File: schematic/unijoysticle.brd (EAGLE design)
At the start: 88.6 x 45.7 mm, 8 parts, among them IC1 4066N, IC2 4066N, IC3 4066N, J1 DB9, J2 DB9, J3 POWER_JACKSLT

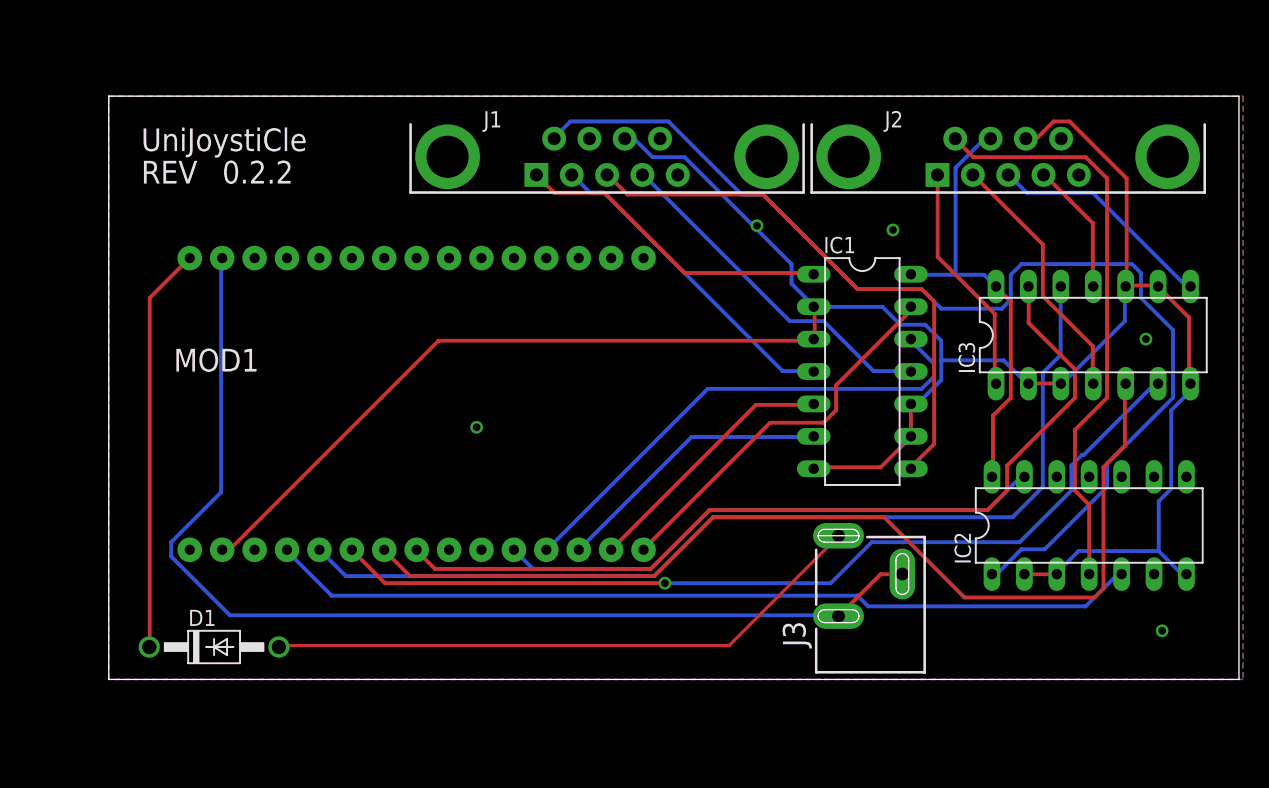
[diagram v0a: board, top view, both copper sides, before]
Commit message: PCB fixes: reduced realstate
uses new DB9 connectors without the uneeded holes.
compabible with Commodore 128D and SX-64
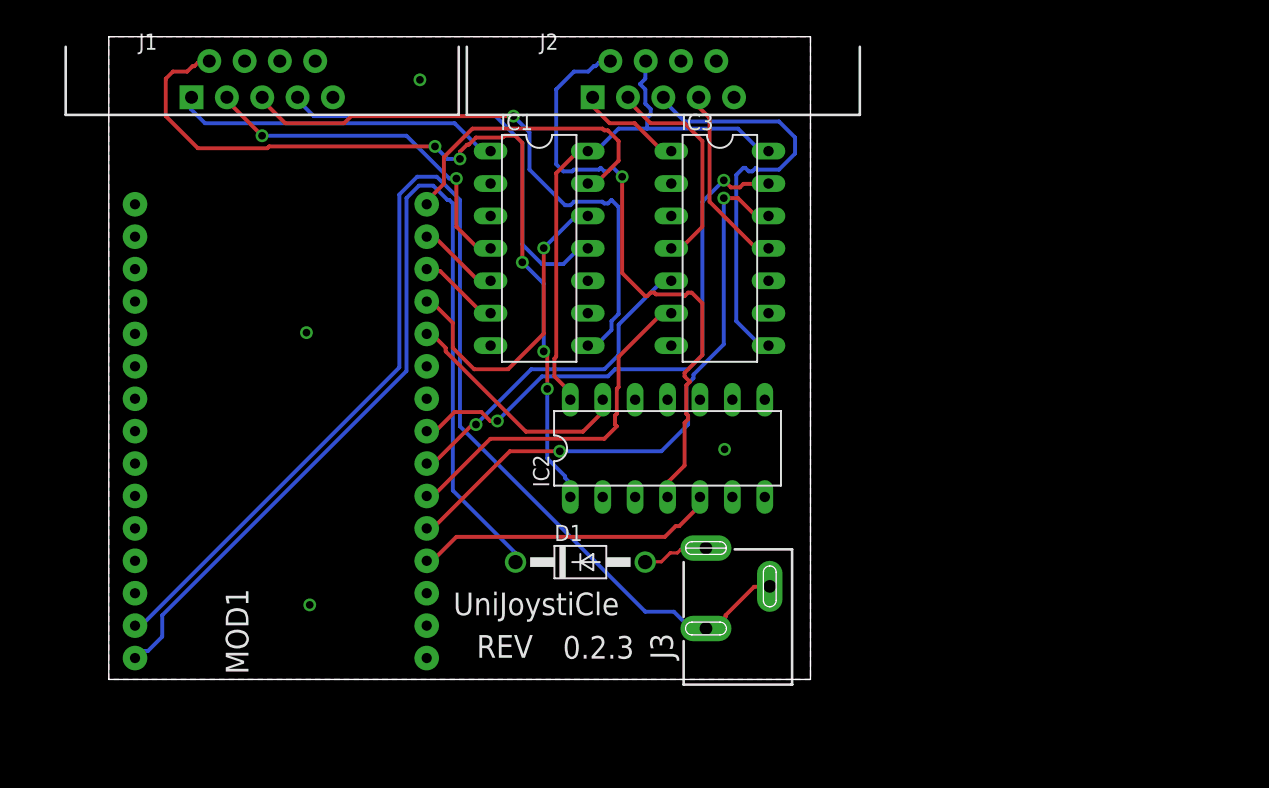
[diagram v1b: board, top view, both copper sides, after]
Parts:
- J1, J2: device SparkFun-Connectors:DB9 -> riq-connectors:DB9
- moved IC2 33.6 mm to (43.8, 18.1)
- moved IC3 30.0 mm to (47.9, 33.8), turned to 270 degrees
- moved D1 29.5 mm to (37.0, 9.19)
- moved J1 27.7 mm to (12.0, 47.0)
- moved J2 27.7 mm to (43.5, 47.0)
- moved IC1 27.1 mm to (33.7, 33.8)
- moved MOD1 10.9 mm to (13.5, 19.5), turned to 0 degrees
- moved J3 10.4 mm to (44.2, -3.51)
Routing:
- net GND: track 184.1 -> 0.00 mm, vias 5 -> 0
- net J2DOWN: track 78.8 -> 26.5 mm, vias 0 -> 1
- net 5V: track 31.8 -> 79.9 mm
- net J2FIRE: track 68.3 -> 23.9 mm
- net J2LEFT: track 71.9 -> 28.3 mm, vias 1 -> 0
- net N$23: track 47.5 -> 5.28 mm
- net J2RIGHT: track 76.7 -> 46.9 mm, vias 0 -> 2
- net J2UP: track 69.2 -> 42.9 mm, vias 0 -> 2
- net J1FIRE: track 43.6 -> 18.7 mm
- net N$21: track 87.3 -> 67.0 mm, vias 0 -> 5
- net J1LEFT: track 22.1 -> 6.45 mm
- net N$15: track 17.9 -> 33.5 mm
- net J1RIGHT: track 39.7 -> 24.9 mm, vias 0 -> 1
- net J1DOWN: track 20.6 -> 6.44 mm
- net 3.3V: track 85.7 -> 98.8 mm
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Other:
- board size 88.6 x 45.7 mm -> 55 x 50.4 mm
- board text added: "2016/08/02"
- board text added: "http://retro.moe"
- board text removed: "2016/06/20"
- board text removed: "https://retro.moe"

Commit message: using wemos d1 mini instead of NodeMCU
smaller realstate PCB making it under 5cm by 5cm.
cheaper to order from certain providers
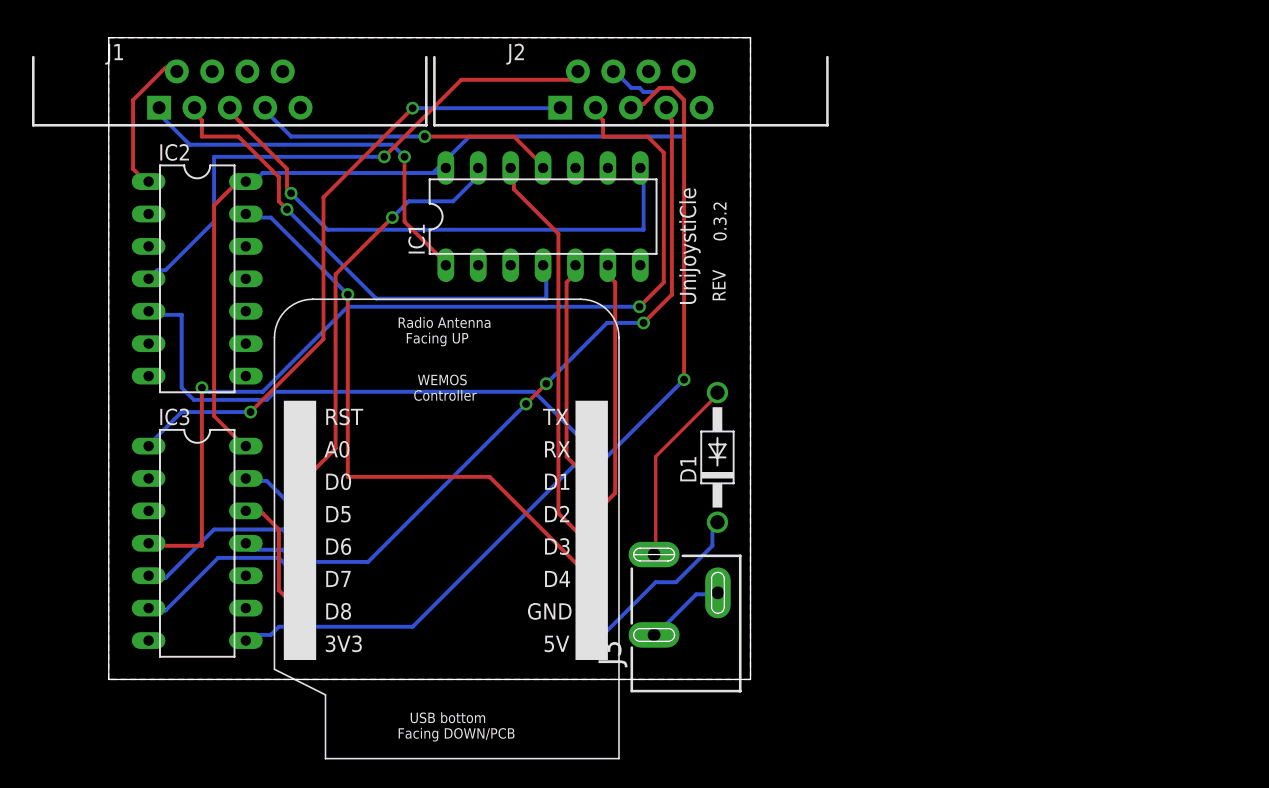
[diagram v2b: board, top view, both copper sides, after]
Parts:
- removed MOD1: ESP12E_DEVKIT, ESP12E_DEVKIT:ESP12E_DEVKIT
- added U$1: WEMOS, 1455413453956-wemos:WEMOS
- moved IC3 47.0 mm to (6.93, 10.7)
- moved IC2 39.2 mm to (6.93, 31.4), turned to 270 degrees
- moved D1 13.5 mm to (47.7, 17.4), turned to 90 degrees
- moved J3 4.10 mm to (40.2, -4.01)
- moved J1 2.67 mm to (9.49, 46.2)
- moved J2 2.67 mm to (40.9, 46.2)
- moved IC1 2.51 mm to (34.0, 36.3), turned to 0 degrees
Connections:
- net 3.3V: no longer MOD1.GND@1
- net 5V: now also U$1.5V; no longer MOD1.VIN
- net GND: now also U$1.GND; no longer MOD1.GND@3
- net J1DOWN: now also U$1.D1; no longer MOD1.D1
- net J1FIRE: now also U$1.D4; no longer MOD1.D4
- net J1LEFT: now also U$1.D2; no longer MOD1.D2
- net J1RIGHT: now also U$1.D3; no longer MOD1.D3
- net J1UP: now also U$1.D0; no longer MOD1.D0
- net J2DOWN: now also U$1.D6; no longer MOD1.D6
- net J2FIRE: now also U$1.RX; no longer MOD1.RX
- net J2LEFT: now also U$1.D7; no longer MOD1.D7
- net J2RIGHT: now also U$1.D8; no longer MOD1.D8
- net J2UP: now also U$1.D5; no longer MOD1.D5
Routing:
- net 3.3V: track 98.8 -> 6.37 mm
- net 5V: track 79.9 -> 14.8 mm
- net N$14: track 17.3 -> 74.7 mm, vias 0 -> 2
- net N$21: track 67.0 -> 11.6 mm, vias 5 -> 0
- net N$16: track 14.7 -> 57.6 mm, vias 0 -> 3
- net N$13: track 8.32 -> 49.8 mm, vias 0 -> 2
- net J2UP: track 42.9 -> 5.47 mm, vias 2 -> 0
- net J2RIGHT: track 46.9 -> 10.4 mm, vias 2 -> 0
- net N$15: track 33.5 -> 70.1 mm, vias 0 -> 1
- net J1FIRE: track 18.7 -> 47.4 mm, vias 0 -> 1
- net VCC: track 43.2 -> 69.8 mm
- net J2FIRE: track 23.9 -> 43.2 mm
- net J1LEFT: track 6.45 -> 20.7 mm
- net J2LEFT: track 28.3 -> 14.4 mm
- net J2DOWN: track 26.5 -> 14.1 mm, vias 1 -> 0
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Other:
- board size 55 x 50.4 mm -> 50.3 x 50.3 mm
- board text removed: "2016/08/02"

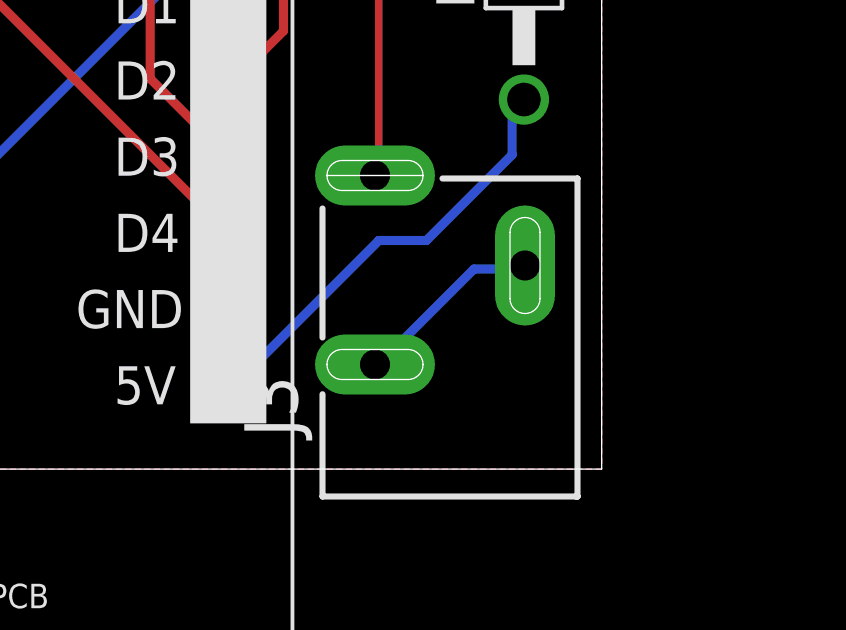
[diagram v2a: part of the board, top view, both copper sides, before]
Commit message: sharing the same ground for all components
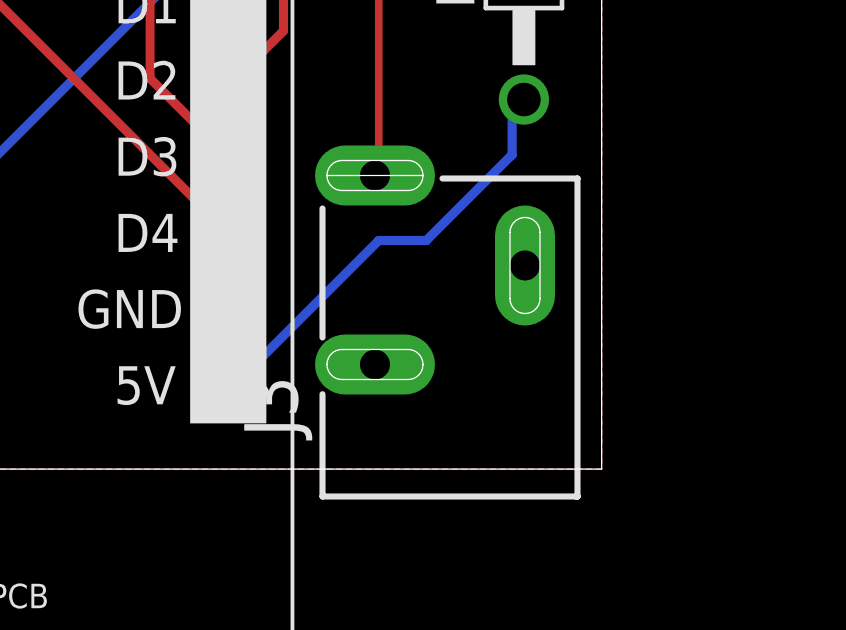
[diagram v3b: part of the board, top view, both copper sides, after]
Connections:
- removed net 3.3V: J3.GND@1, J3.GND@2
- net GND: now also J3.GND@1, J3.GND@2
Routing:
- net 3.3V: track 6.37 -> 0.00 mm
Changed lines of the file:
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@@
 </polygon>
 <contactref element="U$1" pad="GND"/>
+<contactref element="J3" pad="GND@1"/>
+<contactref element="J3" pad="GND@2"/>
 </signal>
 <signal name="VCC">
@@
 <wire x1="47.625" y1="12.065" x2="47.7012" y2="12.319" width="0.3048" layer="16"/>
 </signal>
-<signal name="3.3V">
-<contactref element="J3" pad="GND@1"/>
-<contactref element="J3" pad="GND@2"/>
-<wire x1="46.0375" y1="6.6675" x2="42.8625" y2="3.4925" width="0.3048" layer="16"/>
-<wire x1="47.625" y1="6.6675" x2="46.0375" y2="6.6675" width="0.3048" layer="16"/>
-<wire x1="42.8625" y1="3.4925" x2="42.7374" y2="3.4868" width="0.3048" layer="16"/>
-<wire x1="47.625" y1="6.6675" x2="47.7374" y2="6.7868" width="0.3048" layer="16"/>
-</signal>
 <signal name="J1FIRE">

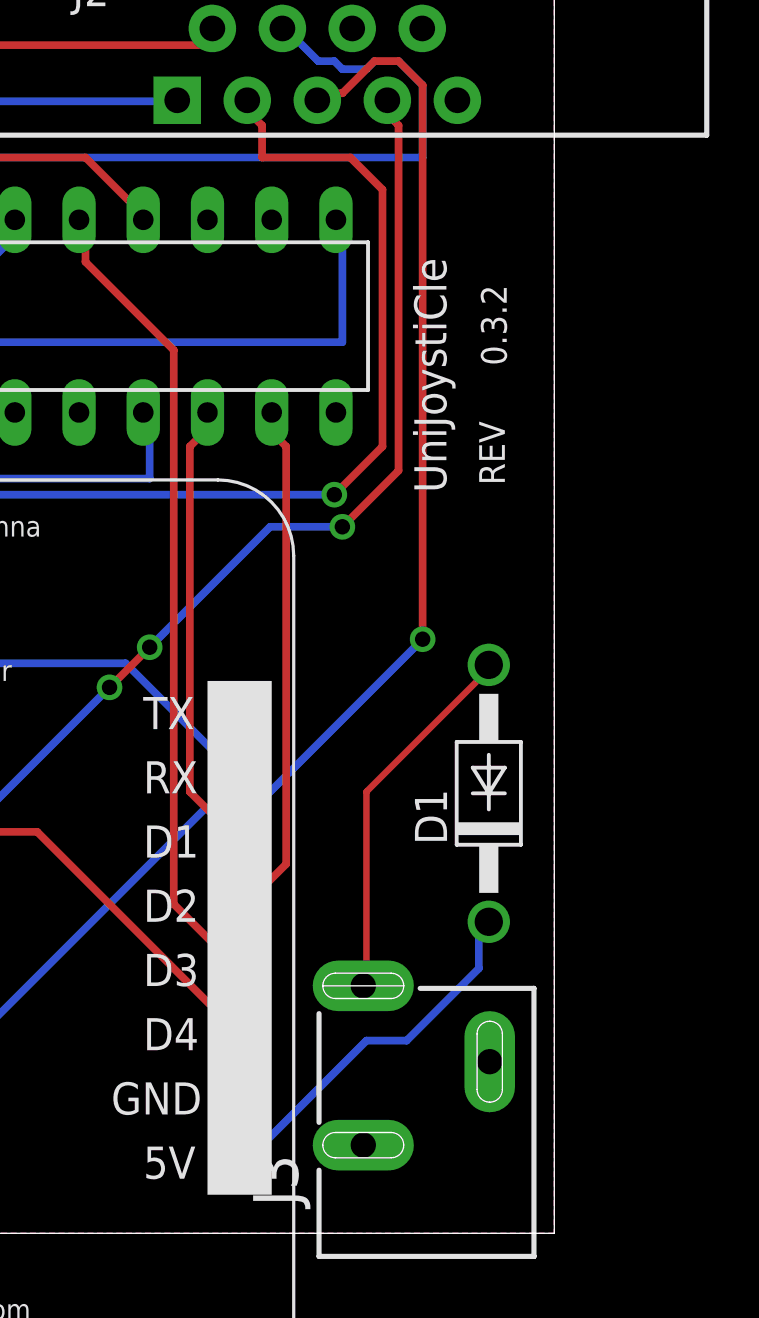
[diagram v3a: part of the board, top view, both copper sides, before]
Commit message: removed diode
apparently not needed:
http://forum.wemos.cc/topic/343/power-the-board-with-both-usb-and-vin-pin-at-the-same-time
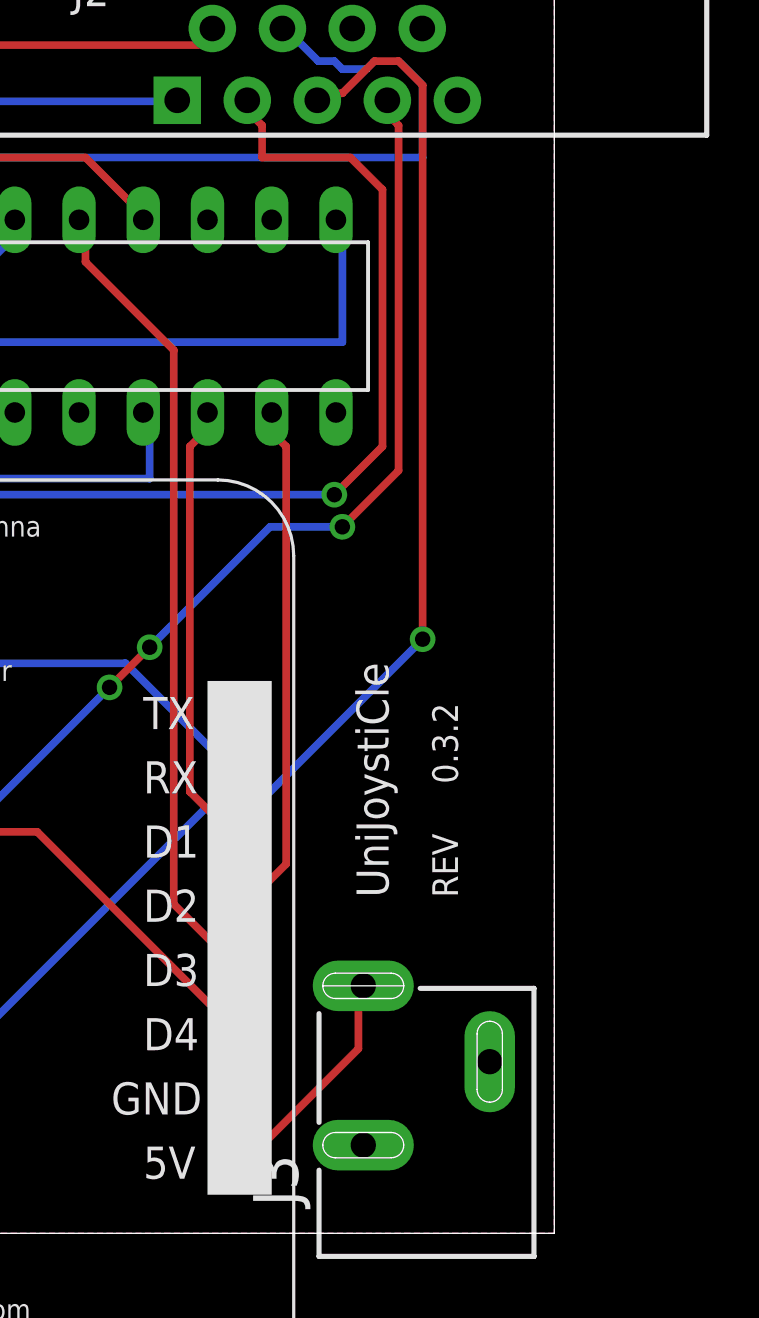
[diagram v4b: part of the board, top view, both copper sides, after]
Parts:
- removed D1: 1N4001, diode:DO41-10
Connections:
- removed net N$23: D1.A, J3.PWR
- net 5V: now also J3.PWR; no longer D1.C
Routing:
- net N$23: track 14.8 -> 0.00 mm
- net 5V: track 14.8 -> 9.10 mm
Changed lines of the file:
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@@
 <wire x1="50.292" y1="50.292" x2="0" y2="50.292" width="0" layer="20"/>
 <wire x1="0" y1="50.292" x2="0" y2="0" width="0" layer="20"/>
-<text x="47.3964" y="34.3154" size="1.016" layer="21" rot="R90" align="top-left">&gt;REVISION</text>
+<text x="45.466" y="17.78" size="1.016" layer="21" rot="R90" align="top-left">&gt;REVISION</text>
 <text x="46.9773" y="25.9715" size="1.27" layer="22" font="vector" rot="SMR270" align="top-right">http://retro.moe</text>
-<text x="47.3202" y="29.591" size="1.016" layer="21" rot="R90" align="top-left">REV</text>
-<text x="44.7548" y="29.2862" size="1.27" layer="21" rot="R90" align="top-left">UniJoystiCle</text>
+<text x="45.466" y="13.2842" size="1.016" layer="21" rot="R90" align="top-left">REV</text>
+<text x="42.4688" y="13.2842" size="1.27" layer="21" rot="R90" align="top-left">UniJoystiCle</text>
 <rectangle x1="33.401" y1="20.3708" x2="33.7058" y2="20.447" layer="22" rot="R90"/>
 <rectangle x1="33.401" y1="20.828" x2="33.7058" y2="20.9042" layer="22" rot="R90"/>
@@
 </autorouter>
 <elements>
-<element name="D1" library="diode" package="DO41-10" value="1N4001" x="47.7012" y="17.399" smashed="yes" rot="R90">
-<attribute name="MPN" value="1N4001" x="47.7012" y="17.399" size="1.778" layer="27" rot="R90" display="off"/>
-<attribute name="MF" value="NTE ELECTRONICS" x="47.7012" y="17.399" size="1.778" layer="27" rot="R90" display="off"/>
-<attribute name="OC_NEWARK" value="10M8464" x="47.7012" y="17.399" size="1.778" layer="27" rot="R90" display="off"/>
-<attribute name="NAME" x="46.0502" y="15.367" size="1.27" layer="25" ratio="10" rot="R90"/>
-</element>
 <element name="IC1" library="40xx" package="DIL14" value="4066N" x="34.036" y="36.2712" smashed="yes">
 <attribute name="MPN" value="SN74HC4066N" x="34.036" y="36.2712" size="1.778" layer="27" display="off"/>
@@
 <via x="21.59" y="40.9575" extent="1-16" drill="0.6096"/>
 </signal>
-<signal name="N$23" class="1">
-<contactref element="D1" pad="A"/>
+<signal name="5V">
+<contactref element="U$1" pad="5V"/>
 <contactref element="J3" pad="PWR"/>
-<wire x1="42.8625" y1="17.4625" x2="47.625" y2="22.225" width="0.254" layer="1"/>
-<wire x1="42.8625" y1="9.8425" x2="42.8625" y2="17.4625" width="0.254" layer="1"/>
-<wire x1="47.625" y1="22.225" x2="47.7012" y2="22.479" width="0.254" layer="1"/>
-<wire x1="42.8625" y1="9.8425" x2="42.7374" y2="9.7868" width="0.254" layer="1"/>
-</signal>
-<signal name="5V">
-<contactref element="D1" pad="C"/>
-<contactref element="U$1" pad="5V"/>
-<wire x1="42.8625" y1="7.62" x2="38.1" y2="2.8575" width="0.3048" layer="16"/>
-<wire x1="44.45" y1="7.62" x2="42.8625" y2="7.62" width="0.3048" layer="16"/>
-<wire x1="47.3075" y1="10.4775" x2="44.45" y2="7.62" width="0.3048" layer="16"/>
-<wire x1="47.3075" y1="12.065" x2="47.3075" y2="10.4775" width="0.3048" layer="16"/>
-<wire x1="47.625" y1="12.065" x2="47.3075" y2="12.065" width="0.3048" layer="16"/>
-<wire x1="38.1" y1="2.8575" x2="37.846" y2="2.794" width="0.3048" layer="16"/>
-<wire x1="47.625" y1="12.065" x2="47.7012" y2="12.319" width="0.3048" layer="16"/>
+<wire x1="42.545" y1="7.3025" x2="38.1" y2="2.8575" width="0.3048" layer="1"/>
+<wire x1="42.545" y1="9.525" x2="42.545" y2="7.3025" width="0.3048" layer="1"/>
+<wire x1="38.1" y1="2.8575" x2="37.846" y2="2.794" width="0.3048" layer="1"/>
+<wire x1="42.545" y1="9.525" x2="42.7374" y2="9.7868" width="0.3048" layer="1"/>
 </signal>
 <signal name="J1FIRE">
